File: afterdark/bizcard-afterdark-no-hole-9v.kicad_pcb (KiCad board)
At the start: 2 copper layers, 35.9 x 20.8 mm, 4 parts

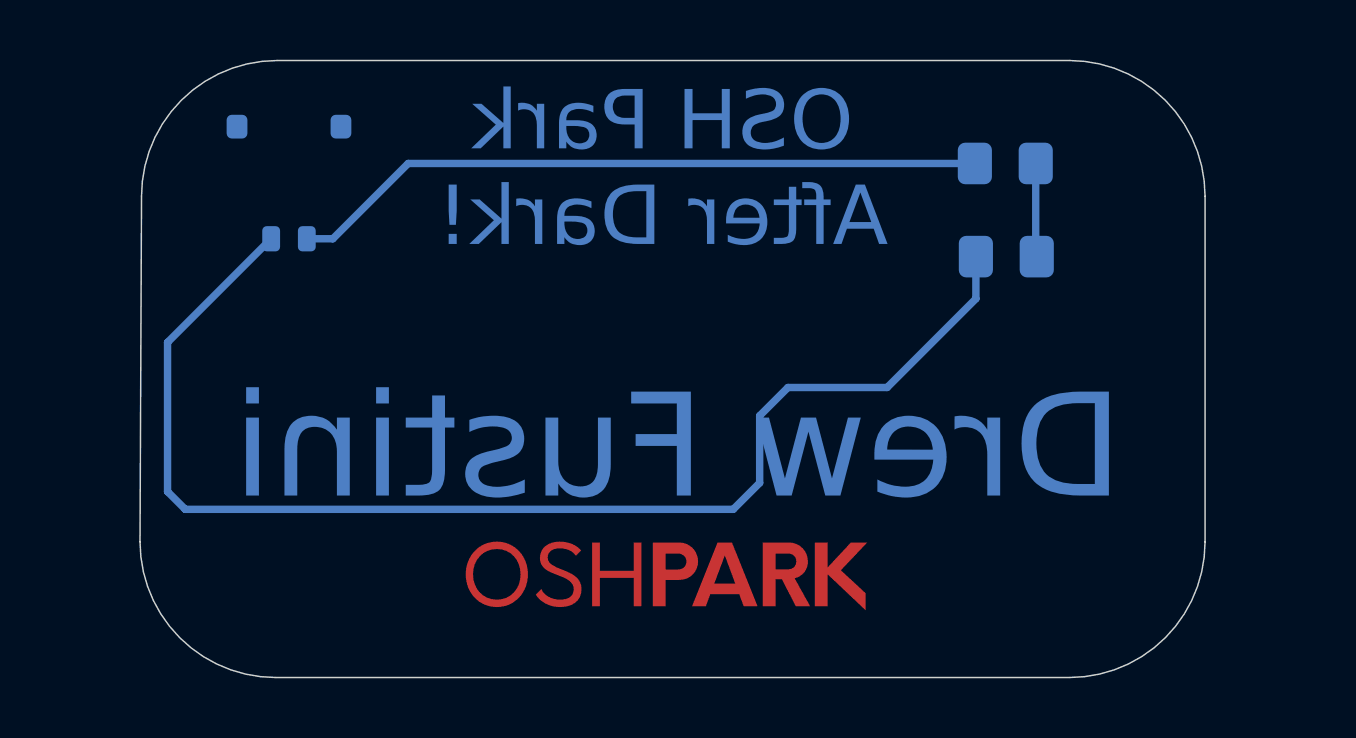
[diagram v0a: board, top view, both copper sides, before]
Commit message: make After Dark with no hole and SMD pads for power
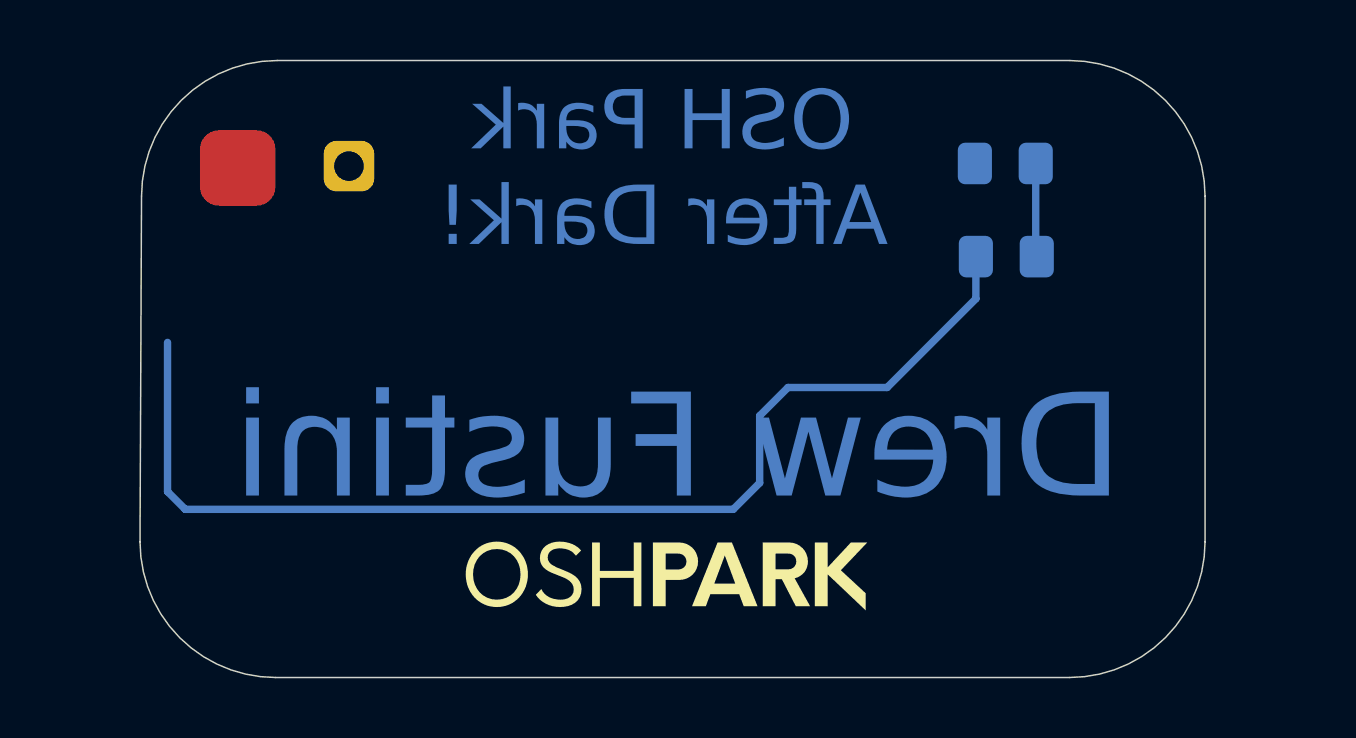
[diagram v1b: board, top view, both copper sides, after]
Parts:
- removed the REF** at (131.7, 65.8)
- added REF**: PinHeader_1x01_P2.54mm_Vertical, afterdark:PinHeader_1x01_P2.54mm_Vertical, F.Cu at (133.7, 65.3)
- added REF**: PinHeader_1x01_P2.54mm_Vertical, afterdark:PinHeader_1x01_P2.54mm_Vertical, F.Cu at (130.0, 65.3)
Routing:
- net (no net): track 69.8 -> 41.4 mm
